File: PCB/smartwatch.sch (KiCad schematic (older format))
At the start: 66 parts, among them U1 STM32F103C8T6, U2 HM-10_MIN, U3 M25P40, U4 BMC150, U5 BMP180, U6 STC4054, U7 NCP551, U8 SH1106, X1 VCHRG, X10 3V3, X2 GND, X3 VBAT, X4 GND, X5 VBAT, X6 VMOT, X7 SWCLK, X8 SWDIO, X9 GND

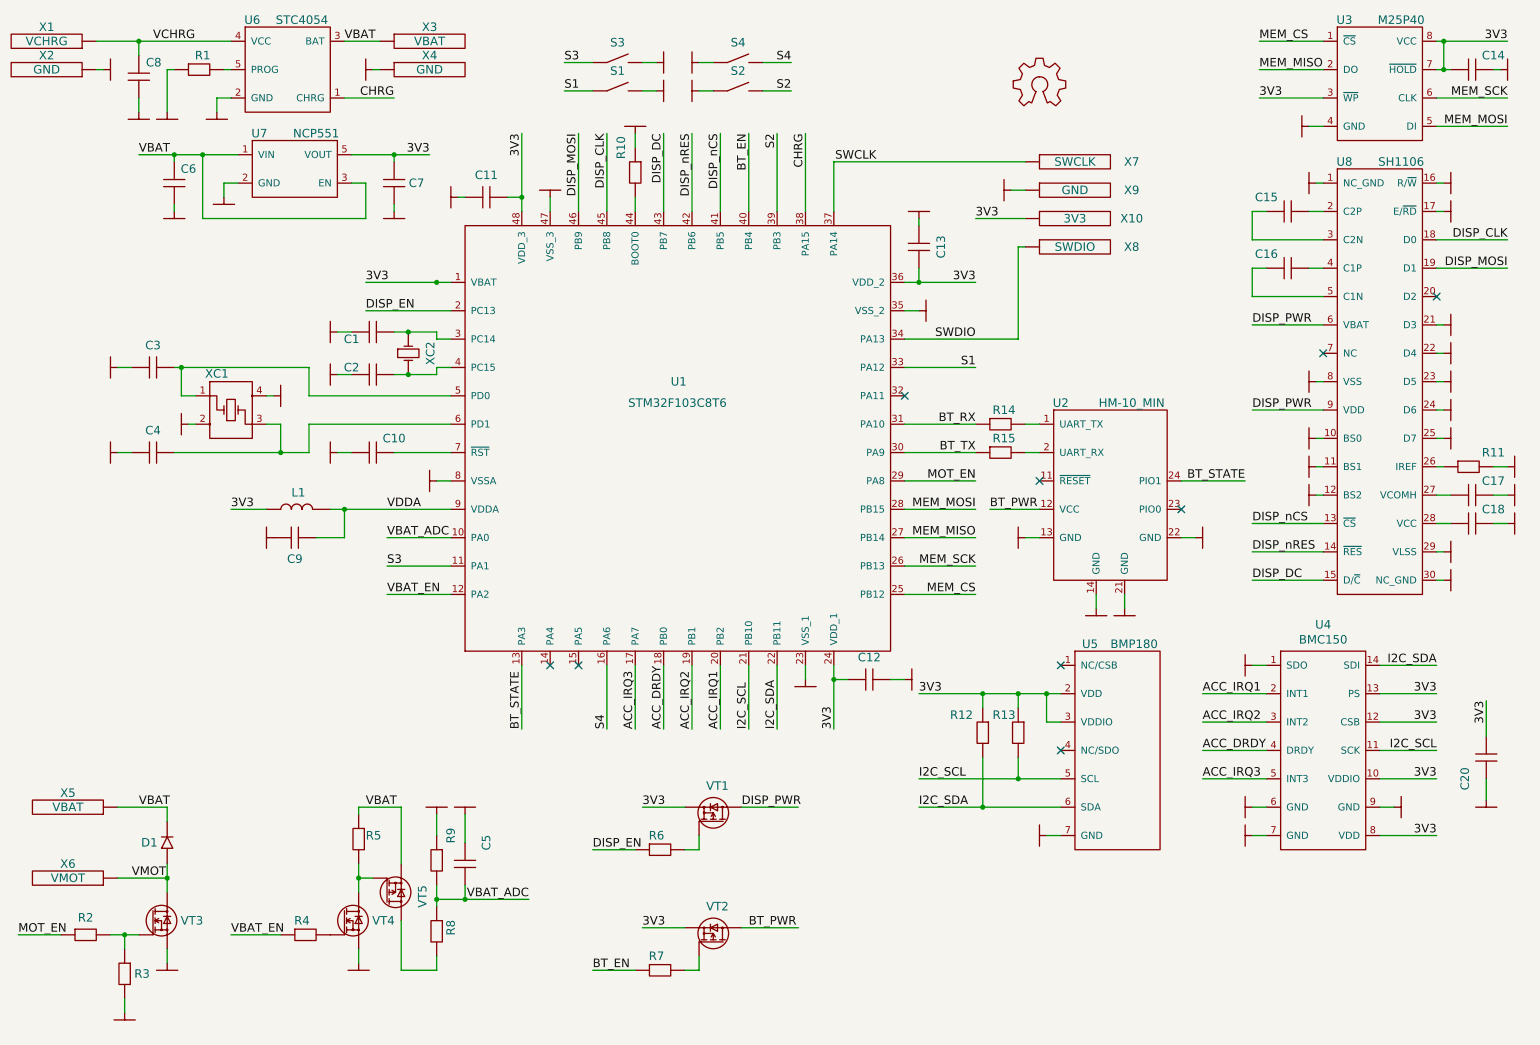
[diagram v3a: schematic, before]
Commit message: PCB: Preparing production files
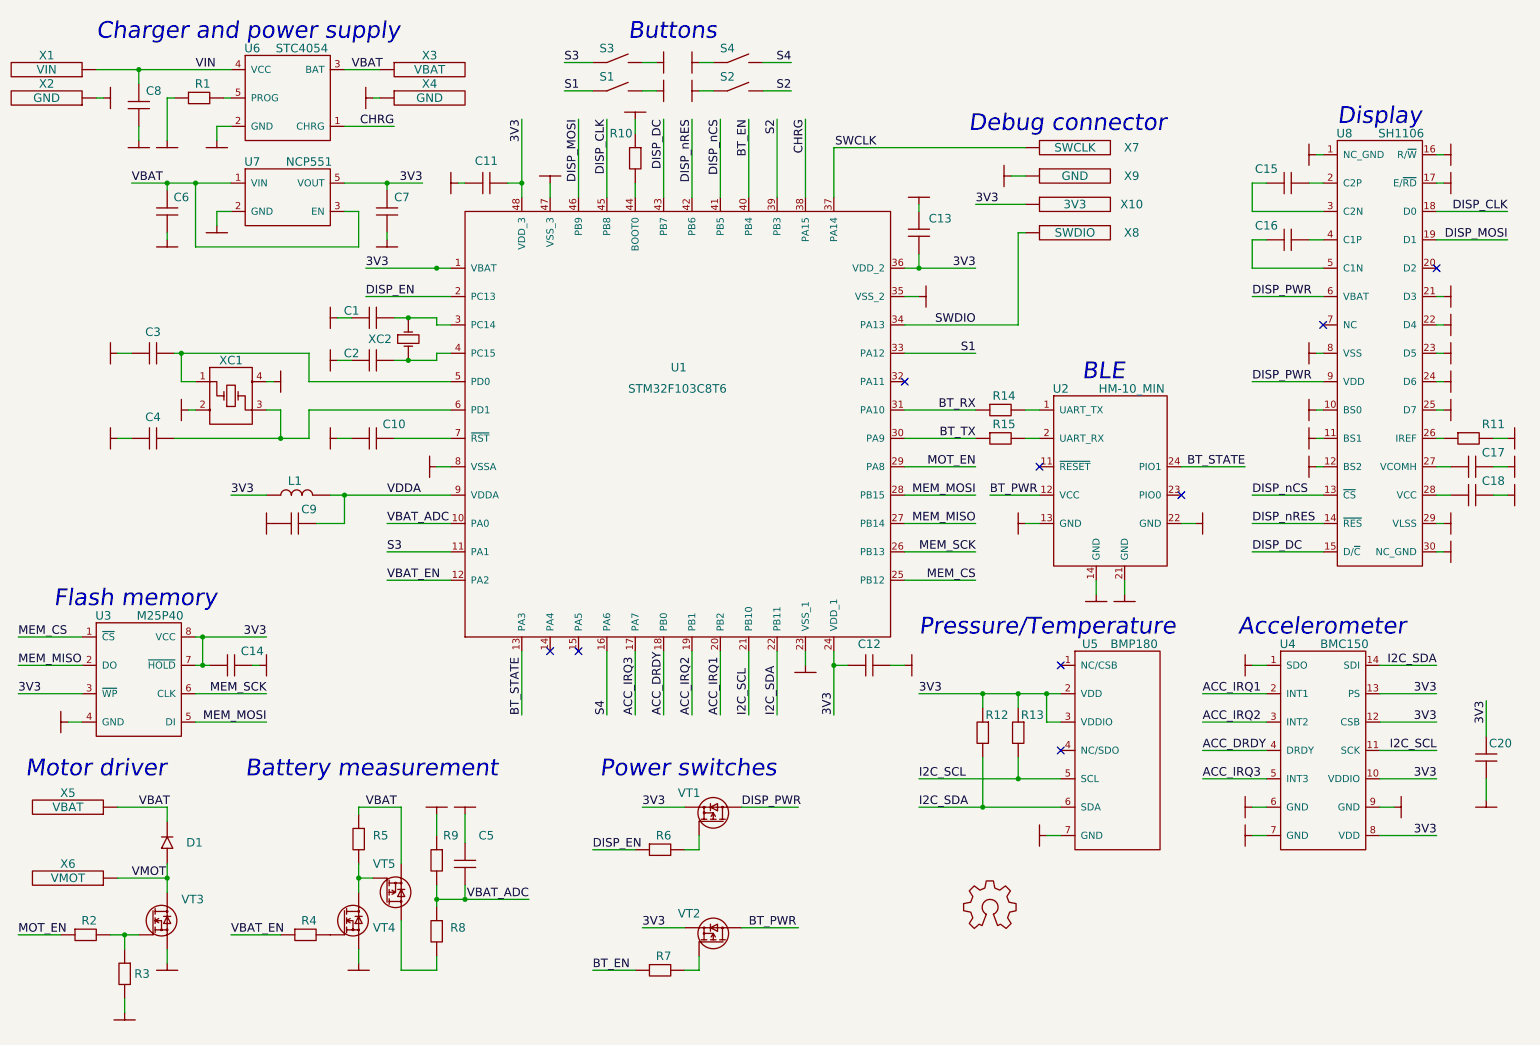
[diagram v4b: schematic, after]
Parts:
- X1: value VCHRG -> VIN
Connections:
- net VCHRG renamed VIN
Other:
- note added: "Accelerometer"
- note added: "BLE"
- note added: "Battery measurement"
- note added: "Buttons"
- note added: "Charger and power supply"
- note added: "Debug connector"
- note added: "Display"
- note added: "Flash memory"
- note added: "Motor driver"
- note added: "Power switches"
- note added: "Pressure/Temperature"
- moved on the sheet: C1, C10, C11, C12, C13, C14, C15, C16, C17, C18, C2, C3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

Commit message: Values update
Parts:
- C1, C2, C3, C4: value capacitor -> 15p
- C6, C7: value capacitor -> 0.1
- R1: value resistor -> 10k
- R12, R13: value resistor -> 1k
- R14, R15: value 390k -> 10k
- R2, R4, R6, R7: value resistor -> 100
- R3: value resistor -> 100k
- XC2: value CRYSTAL_2pin -> 32768
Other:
- note added: "Ichg = 100mA"
- moved on the sheet: C1, C2, C3, C4, XC1, XC2

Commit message: GPIO class, draft SW SPI and display classes
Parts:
- C11: value capacitor -> 22u
- C12, C13, C20, C5: value capacitor -> 0.1
- R10: value resistor -> 1k
- R5, R8, R9: value resistor -> 10k
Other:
- note added: "I2C2"
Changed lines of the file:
@@
 U 1 1 57056E63
 P 3000 6150
-F 0 "R5" V 3150 6250 60  0000 L CNN
-F 1 "resistor" H 3150 6050 60  0001 C CNN
+F 0 "R5" V 3100 6300 60  0000 C CNN
+F 1 "10k" V 3200 6300 60  0000 C CNN
 F 2 "discrete_SMD:0402_R" H 3000 6150 60  0001 C CNN
 F 3 "" H 3000 6150 60  0000 C CNN
@@
 U 1 1 57058D40
 P 3550 6300
-F 0 "R9" V 3550 6400 60  0000 C CNN
-F 1 "resistor" H 3700 6200 60  0001 C CNN
+F 0 "R9" V 3650 6150 60  0000 C CNN
+F 1 "10k" V 3750 6150 60  0000 C CNN
 F 2 "discrete_SMD:0402_R" H 3550 6300 60  0001 C CNN
 F 3 "" H 3550 6300 60  0000 C CNN
@@
 U 1 1 57058DF9
 P 3550 6800
-F 0 "R8" V 3700 6950 60  0000 C CNN
-F 1 "resistor" H 3700 6700 60  0001 C CNN
+F 0 "R8" V 3650 6950 60  0000 C CNN
+F 1 "10k" V 3750 6950 60  0000 C CNN
 F 2 "discrete_SMD:0402_R" H 3550 6800 60  0001 C CNN
 F 3 "" H 3550 6800 60  0000 C CNN
@@
 U 1 1 570594EB
 P 3750 6350
-F 0 "C5" V 3700 6500 60  0000 C CNN
-F 1 "capacitor" H 3900 6250 60  0001 C CNN
+F 0 "C5" V 3800 6550 60  0000 C CNN
+F 1 "0.1" V 3900 6550 60  0000 C CNN
 F 2 "discrete_SMD:0402_C" H 3750 6350 60  0001 C CNN
 F 3 "" H 3750 6350 60  0000 C CNN
@@
 P 6450 5100
 F 0 "C12" H 6600 5250 60  0000 C CNN
-F 1 "capacitor" H 6600 5000 60  0001 C CNN
+F 1 "0.1" H 6600 4950 60  0000 C CNN
 F 2 "discrete_SMD:0402_C" H 6450 5100 60  0001 C CNN
 F 3 "" H 6450 5100 60  0000 C CNN
@@
 P 6950 2200
 F 0 "C13" V 7200 2050 60  0000 C CNN
-F 1 "capacitor" H 7100 2100 60  0001 C CNN
+F 1 "0.1" V 7000 2050 60  0000 C CNN
 F 2 "discrete_SMD:0402_C" H 6950 2200 60  0001 C CNN
 F 3 "" H 6950 2200 60  0000 C CNN
@@
 P 4050 1700
 F 0 "C11" H 4200 1544 60  0000 C CNN
-F 1 "capacitor" H 4200 1600 60  0001 C CNN
+F 1 "22u" H 4200 1850 60  0000 C CNN
 F 2 "discrete_SMD:0603_C" H 4050 1700 60  0001 C CNN
 F 3 "" H 4050 1700 60  0000 C CNN
@@
 P 4950 1350
 F 0 "R10" V 4950 1250 60  0000 C CNN
-F 1 "resistor" H 5100 1250 60  0001 C CNN
+F 1 "1k" V 5250 1250 60  0000 C CNN
 F 2 "discrete_SMD:0402_R" H 4950 1350 60  0001 C CNN
 F 3 "" H 4950 1350 60  0000 C CNN
@@
 P 10950 5900
 F 0 "C20" V 11200 5800 60  0000 C CNN
-F 1 "capacitor" H 11100 5800 60  0001 C CNN
+F 1 "0.1" V 11000 5800 60  0000 C CNN
 F 2 "discrete_SMD:0402_C" H 10950 5900 60  0001 C CNN
 F 3 "" H 10950 5900 60  0000 C CNN
@@
 	3350 2900 3650 2900
 Wire Wire Line
-	3350 2900 3350 2950
+	3350 2950 3350 2900
 Connection ~ 3550 2300
 Wire Wire Line
@@
 Wire Wire Line
 	2450 3500 2450 3300
+Text Notes 6100 5600 0    60   ~ 0
+I2C2
+Wire Notes Line
+	5750 5450 5900 5600
+Wire Notes Line
+	5900 5600 6350 5600
+Wire Notes Line
+	5950 5450 6100 5600
 $EndSCHEMATC

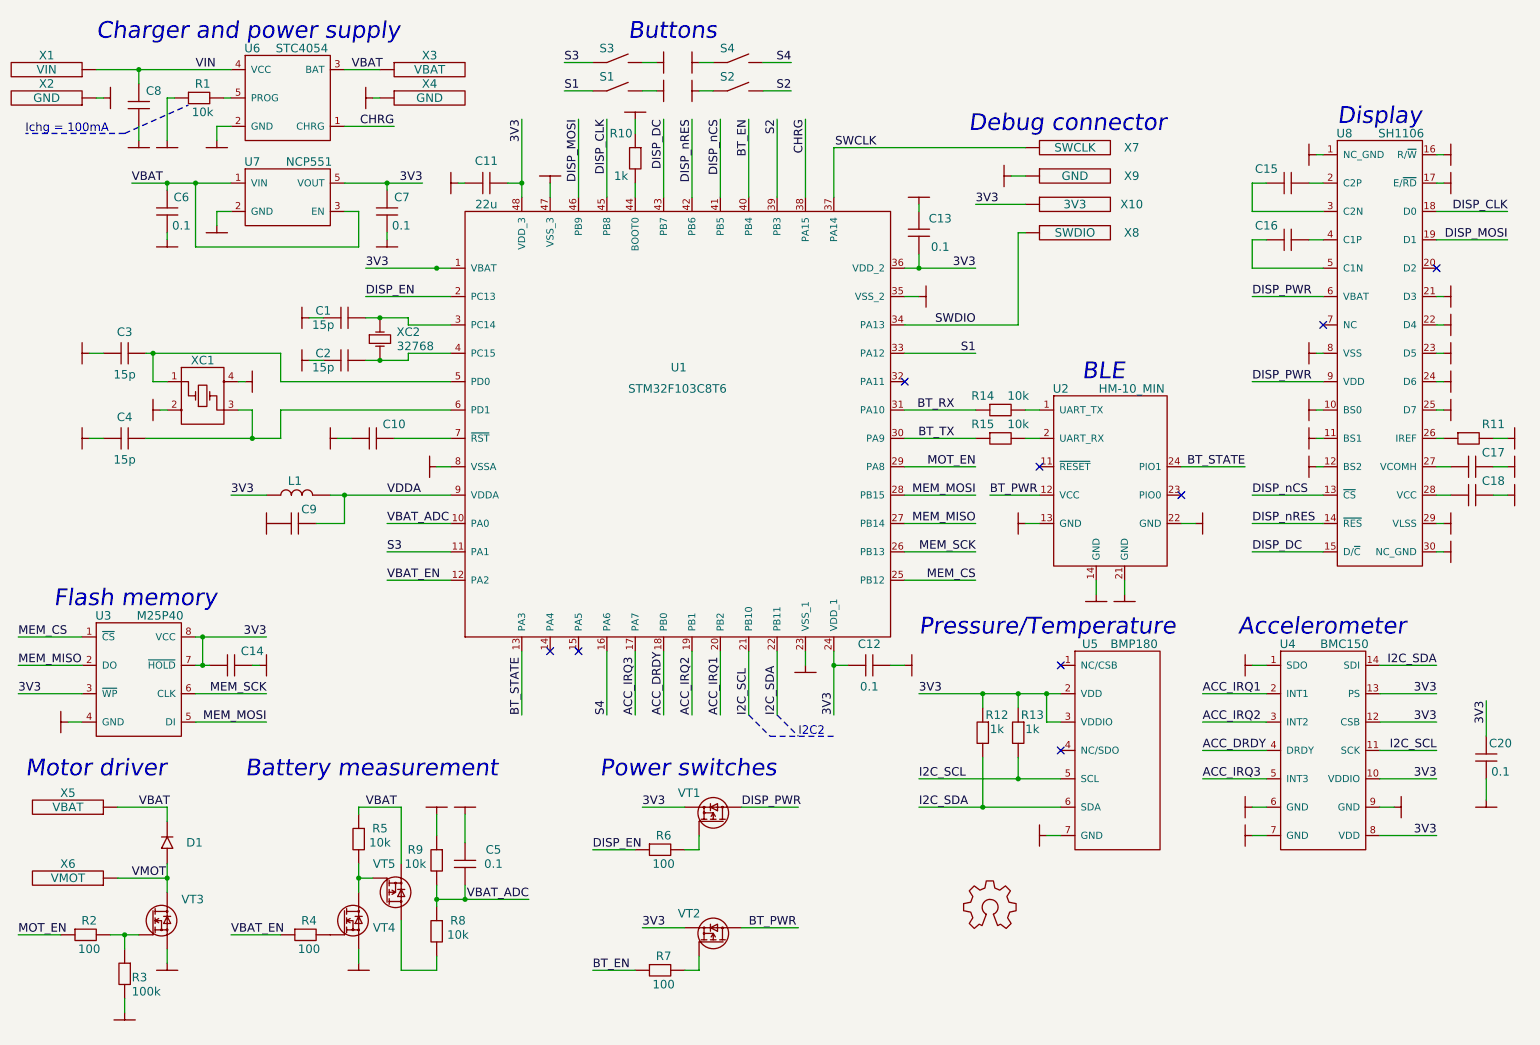
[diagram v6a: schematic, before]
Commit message: PCB component values update
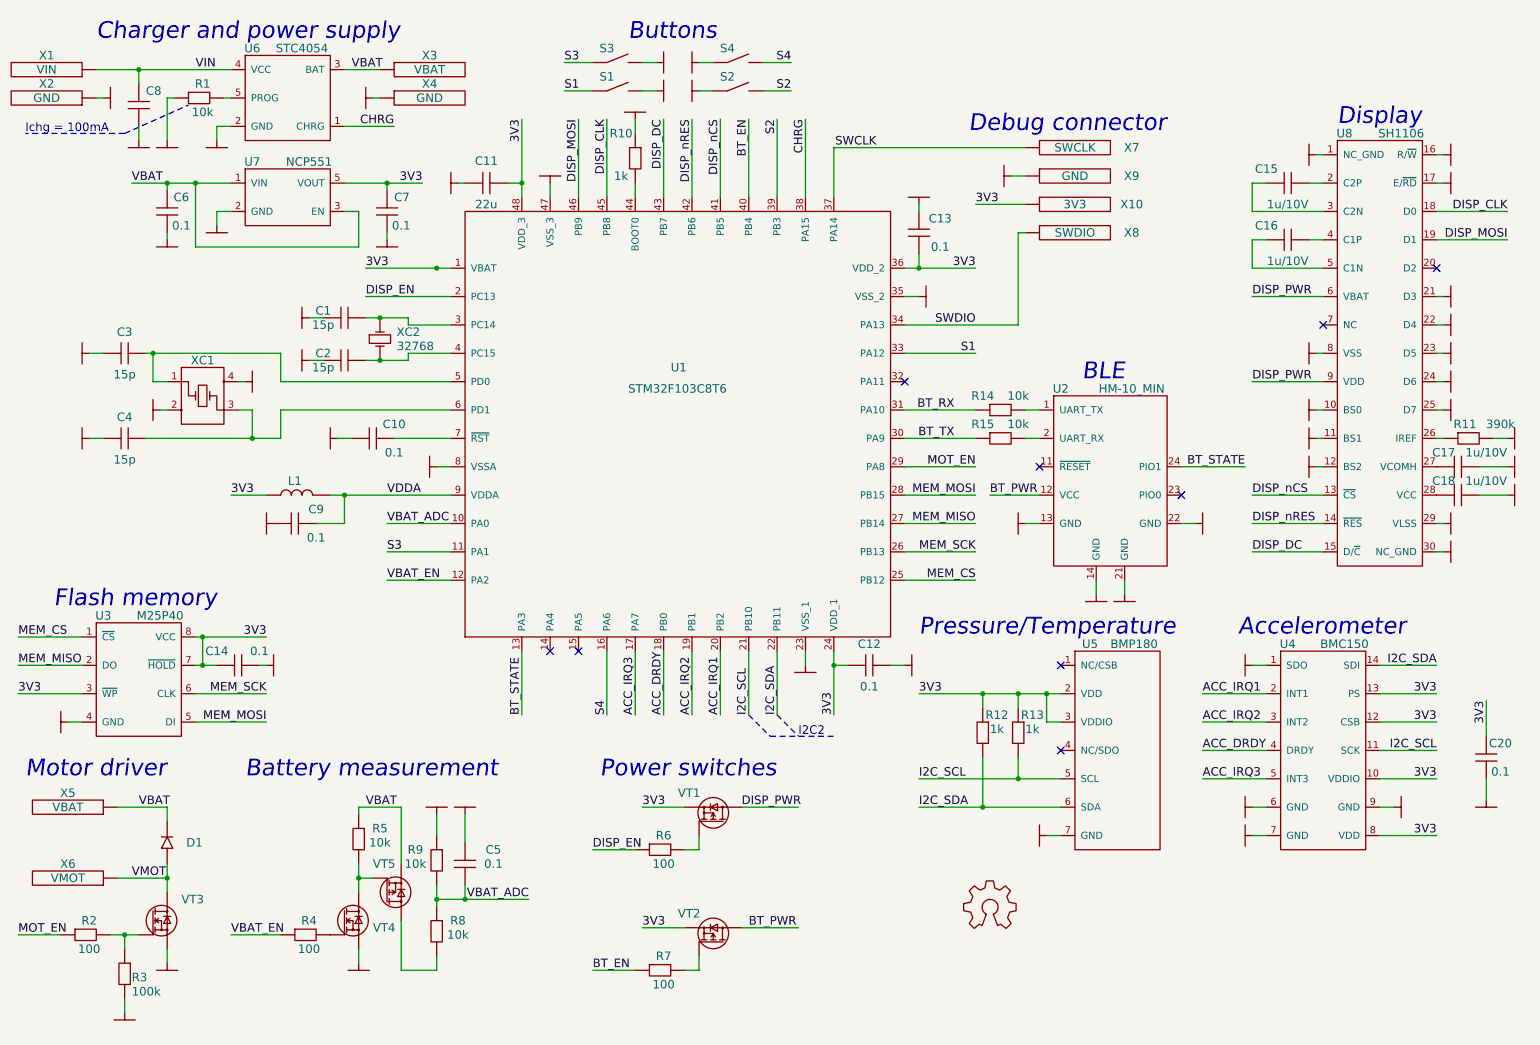
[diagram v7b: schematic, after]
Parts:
- C10, C14, C9: value capacitor -> 0.1
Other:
- moved on the sheet: C14, C17, C18
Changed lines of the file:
@@
 P 2950 3500
 F 0 "C10" H 3250 3600 60  0000 C CNN
-F 1 "capacitor" H 3100 3400 60  0001 C CNN
+F 1 "0.1" H 3250 3400 60  0000 C CNN
 F 2 "discrete_SMD:0402_C" H 2950 3500 60  0001 C CNN
 F 3 "" H 2950 3500 60  0000 C CNN
@@
 U 1 1 57061B34
 P 2400 4100
-F 0 "C9" H 2650 4200 60  0000 C CNN
-F 1 "capacitor" H 2550 4000 60  0001 C CNN
+F 0 "C9" H 2700 4200 60  0000 C CNN
+F 1 "0.1" H 2700 4000 60  0000 C CNN
 F 2 "discrete_SMD:0402_C" H 2400 4100 60  0001 C CNN
 F 3 "" H 2400 4100 60  0000 C CNN
@@
 L capacitor C14
 U 1 1 57099636
-P 2250 5100
-F 0 "C14" H 2250 5000 60  0000 C CNN
-F 1 "capacitor" H 2400 5000 60  0001 C CNN
-F 2 "discrete_SMD:0402_C" H 2250 5100 60  0001 C CNN
-F 3 "" H 2250 5100 60  0000 C CNN
-	1    2250 5100
+P 2300 5100
+F 0 "C14" H 2600 5000 60  0000 C CNN
+F 1 "0.1" H 2300 5000 60  0000 C CNN
+F 2 "discrete_SMD:0402_C" H 2300 5100 60  0001 C CNN
+F 3 "" H 2300 5100 60  0000 C CNN
+	1    2300 5100
 	-1   0    0    1
 $EndComp
@@
 L GND #PWR030
 U 1 1 57099C1C
-P 2300 5100
-F 0 "#PWR030" H 2300 4950 50  0001 C CNN
-F 1 "GND" H 2300 5000 50  0001 C CNN
-F 2 "" H 2300 5100 60  0000 C CNN
-F 3 "" H 2300 5100 60  0000 C CNN
-	1    2300 5100
+P 2350 5100
+F 0 "#PWR030" H 2350 4950 50  0001 C CNN
+F 1 "GND" H 2350 5000 50  0001 C CNN
+F 2 "" H 2350 5100 60  0000 C CNN
+F 3 "" H 2350 5100 60  0000 C CNN
+	1    2350 5100
 	0    -1   -1   0
 $EndComp
@@
 P 9400 1700
 F 0 "C15" H 9400 1800 60  0000 C CNN
-F 1 "1u/10V" H 9550 1600 60  0001 C CNN
+F 1 "1u/10V" H 9550 1550 60  0000 C CNN
 F 2 "discrete_SMD:0603_C" H 9400 1700 60  0001 C CNN
 F 3 "" H 9400 1700 60  0000 C CNN
@@
 P 9400 2100
 F 0 "C16" H 9400 2200 60  0000 C CNN
-F 1 "1u/10V" H 9550 2000 60  0001 C CNN
+F 1 "1u/10V" H 9550 1950 60  0000 C CNN
 F 2 "discrete_SMD:0603_C" H 9400 2100 60  0001 C CNN
 F 3 "" H 9400 2100 60  0000 C CNN
@@
 U 1 1 570A1928
 P 10650 3500
-F 0 "R11" H 11000 3600 60  0000 C CNN
-F 1 "390k" H 10800 3400 60  0001 C CNN
+F 0 "R11" H 10800 3600 60  0000 C CNN
+F 1 "390k" H 11050 3600 60  0000 C CNN
 F 2 "discrete_SMD:0402_R" H 10650 3500 60  0001 C CNN
 F 3 "" H 10650 3500 60  0000 C CNN
@@
 L capacitor C17
 U 1 1 570A364C
-P 10700 3700
-F 0 "C17" H 11000 3800 60  0000 C CNN
-F 1 "1u/10V" H 10850 3600 60  0001 C CNN
-F 2 "discrete_SMD:0603_C" H 10700 3700 60  0001 C CNN
-F 3 "" H 10700 3700 60  0000 C CNN
-	1    10700 3700
+P 10600 3700
+F 0 "C17" H 10650 3800 60  0000 C CNN
+F 1 "1u/10V" H 10950 3800 60  0000 C CNN
+F 2 "discrete_SMD:0603_C" H 10600 3700 60  0001 C CNN
+F 3 "" H 10600 3700 60  0000 C CNN
+	1    10600 3700
 	1    0    0    -1
 $EndComp
@@
 L capacitor C18
 U 1 1 570A380B
-P 10700 3900
-F 0 "C18" H 11000 4000 60  0000 C CNN
-F 1 "1u/10V" H 10850 3800 60  0001 C CNN
-F 2 "discrete_SMD:0603_C" H 10700 3900 60  0001 C CNN
-F 3 "" H 10700 3900 60  0000 C CNN
-	1    10700 3900
+P 10600 3900
+F 0 "C18" H 10650 4000 60  0000 C CNN
+F 1 "1u/10V" H 10950 4000 60  0000 C CNN
+F 2 "discrete_SMD:0603_C" H 10600 3900 60  0001 C CNN
+F 3 "" H 10600 3900 60  0000 C CNN
+	1    10600 3900
 	1    0    0    -1
 $EndComp
@@
 	1850 4900 2350 4900
 Wire Wire Line
-	1850 5100 1950 5100
+	1850 5100 2000 5100
 Wire Wire Line
 	1900 5100 1900 4900
@@
 	10650 3300 10600 3300
 Wire Wire Line
-	10600 3700 10700 3700
-Wire Wire Line
-	10600 3900 10700 3900
-Wire Wire Line
-	11000 3700 11100 3700
-Wire Wire Line
-	11100 3900 11000 3900
+	10600 3700 10600 3700
+Wire Wire Line
+	10600 3900 10600 3900
+Wire Wire Line
+	10900 3700 11100 3700
+Wire Wire Line
+	11100 3900 10900 3900
 Wire Wire Line
 	10600 4100 10650 4100
@@
 Connection ~ 3550 2300
 Wire Wire Line
-	2300 5100 2250 5100
+	2350 5100 2300 5100
 Connection ~ 1900 5100
 Wire Wire Line
